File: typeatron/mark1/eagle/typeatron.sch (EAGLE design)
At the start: 24 parts

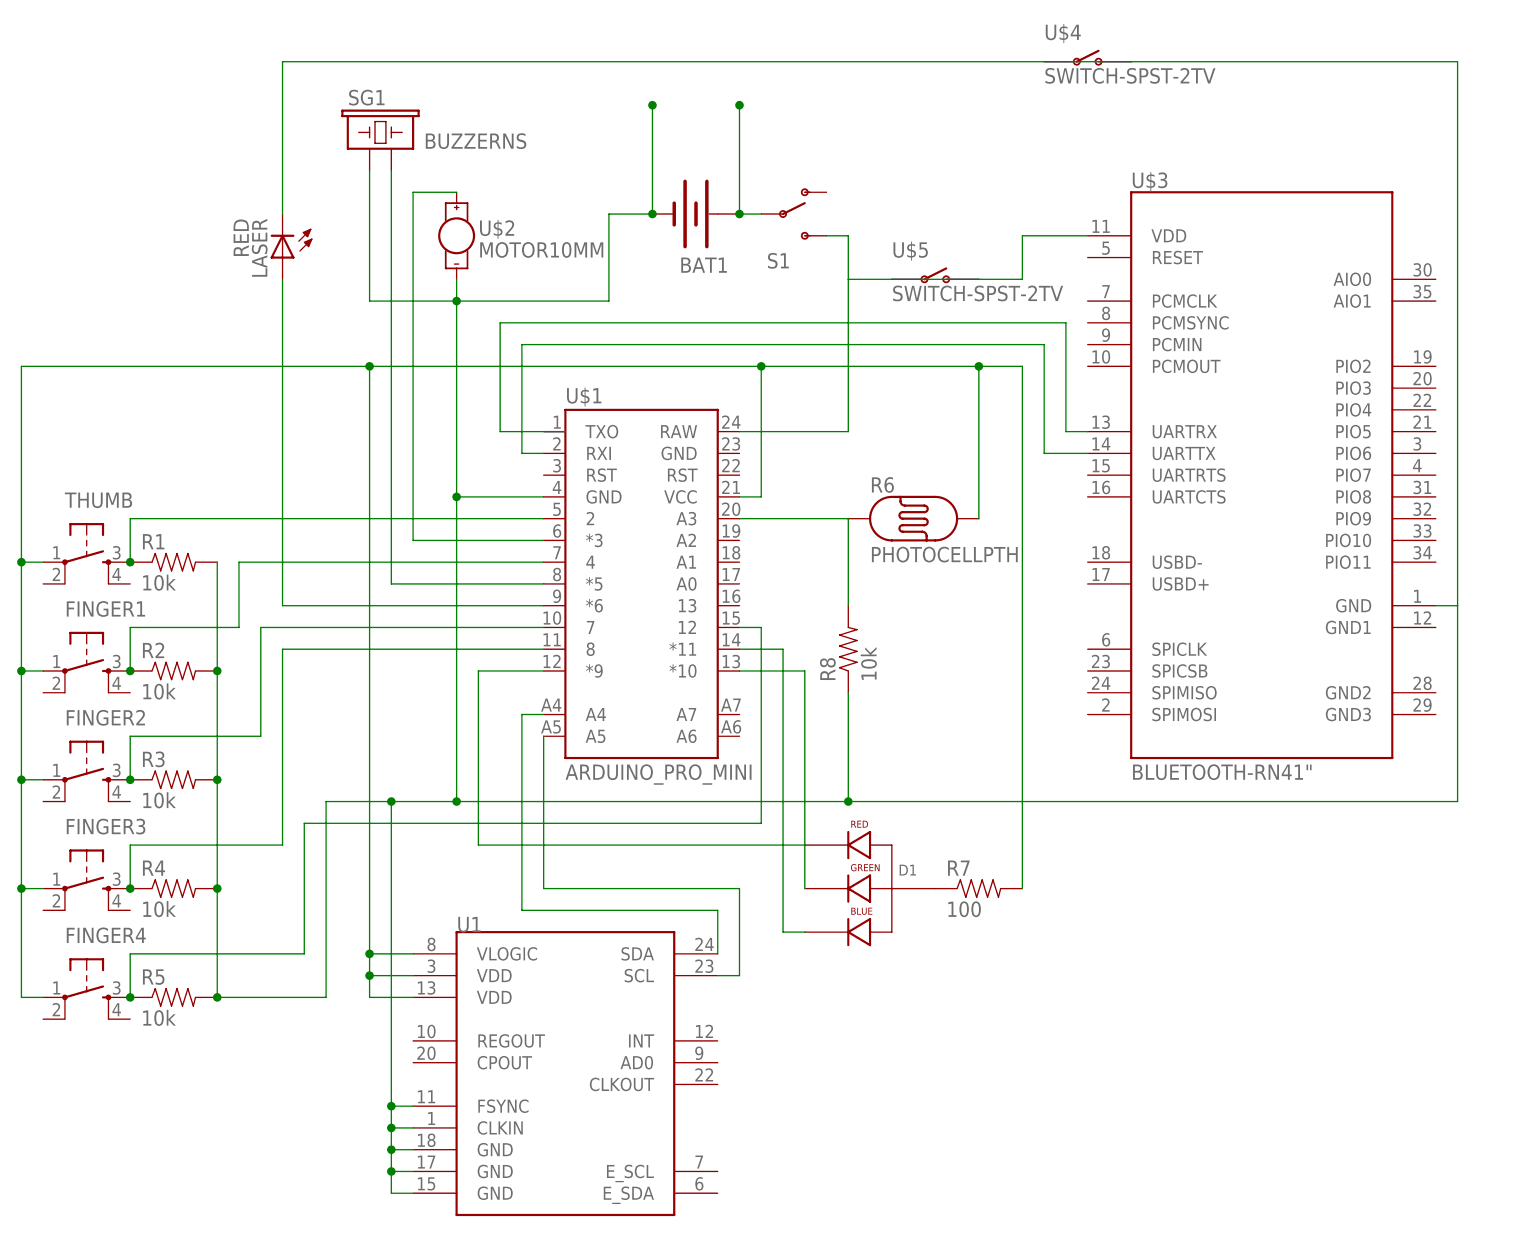
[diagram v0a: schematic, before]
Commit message: Adjusted Typeatron's jumper locations in schematic
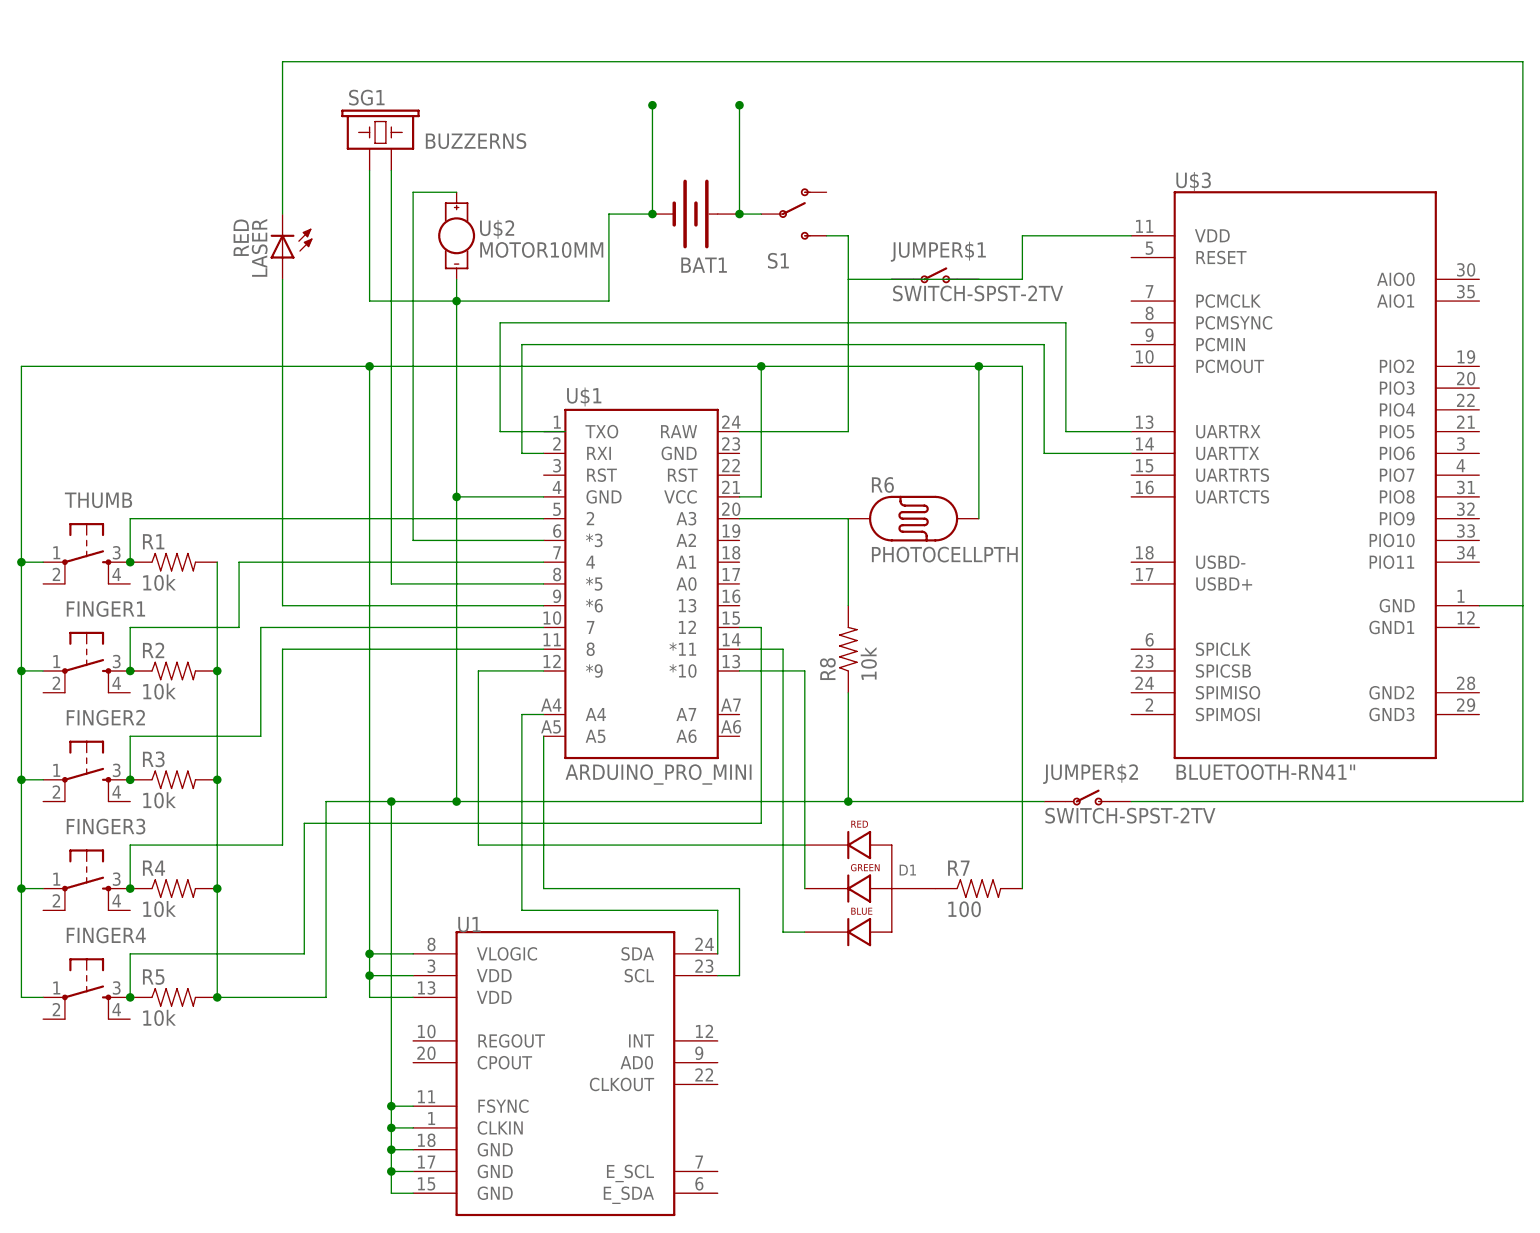
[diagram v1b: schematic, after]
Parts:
- removed U$4: SWITCH-SPST-2TV, SparkFun-Electromechanical:SWITCH-SPST-2TV
- added JUMPER$2: SWITCH-SPST-2TV, SparkFun-Electromechanical:SWITCH-SPST-2TV
- renumbered U$5 to JUMPER$1
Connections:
- new net N$9: JUMPER$2.O, LASER.C, U$3.GND
- net N$3: now also JUMPER$2.P; no longer LASER.C, U$3.GND, U$4.O, U$4.P
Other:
- moved on the sheet: U$3
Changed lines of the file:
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@@
 <part name="R8" library="SparkFun-Resistors" deviceset="10KOHM1/6W5%(PTH)" device="KIT" value="10k"/>
 <part name="LASER" library="SparkFun-LED" deviceset="LED-RED" device="0603" value="RED"/>
-<part name="U$4" library="SparkFun-Electromechanical" deviceset="SWITCH-SPST-2" device="TV"/>
-<part name="U$5" library="SparkFun-Electromechanical" deviceset="SWITCH-SPST-2" device="TV"/>
+<part name="JUMPER$1" library="SparkFun-Electromechanical" deviceset="SWITCH-SPST-2" device="TV"/>
+<part name="JUMPER$2" library="SparkFun-Electromechanical" deviceset="SWITCH-SPST-2" device="TV"/>
 </parts>
 <sheets>
@@
 <instance part="SG1" gate="G$1" x="30.48" y="114.3"/>
 <instance part="U$2" gate="G$1" x="40.64" y="104.14"/>
-<instance part="U$3" gate="G$1" x="134.62" y="76.2"/>
+<instance part="U$3" gate="G$1" x="139.7" y="76.2"/>
 <instance part="BAT1" gate="G$1" x="68.58" y="106.68" rot="R180"/>
 <instance part="R6" gate="G$1" x="93.98" y="71.12"/>
@@
 <instance part="R8" gate="G$1" x="86.36" y="55.88" rot="R90"/>
 <instance part="LASER" gate="G$1" x="20.32" y="101.6" rot="R180"/>
-<instance part="U$4" gate="G$1" x="114.3" y="124.46"/>
-<instance part="U$5" gate="G$1" x="96.52" y="99.06"/>
+<instance part="JUMPER$1" gate="G$1" x="96.52" y="99.06"/>
+<instance part="JUMPER$2" gate="G$1" x="114.3" y="38.1"/>
 </instances>
 <busses>
@@
 <wire x1="83.82" y1="104.14" x2="86.36" y2="104.14" width="0.1524" layer="91"/>
 <wire x1="86.36" y1="104.14" x2="86.36" y2="99.06" width="0.1524" layer="91"/>
-<pinref part="U$5" gate="G$1" pin="O"/>
-<pinref part="U$5" gate="G$1" pin="P"/>
+<pinref part="JUMPER$1" gate="G$1" pin="O"/>
+<pinref part="JUMPER$1" gate="G$1" pin="P"/>
 <wire x1="91.44" y1="99.06" x2="101.6" y2="99.06" width="0.1524" layer="91"/>
 <wire x1="86.36" y1="99.06" x2="91.44" y2="99.06" width="0.1524" layer="91"/>
@@
 <wire x1="106.68" y1="99.06" x2="106.68" y2="104.14" width="0.1524" layer="91"/>
 <pinref part="U$3" gate="G$1" pin="VDD"/>
-<wire x1="106.68" y1="104.14" x2="114.3" y2="104.14" width="0.1524" layer="91"/>
+<wire x1="106.68" y1="104.14" x2="119.38" y2="104.14" width="0.1524" layer="91"/>
 </segment>
 </net>
@@
 <segment>
 <pinref part="U$3" gate="G$1" pin="UARTTX"/>
-<wire x1="114.3" y1="78.74" x2="109.22" y2="78.74" width="0.1524" layer="91"/>
+<wire x1="119.38" y1="78.74" x2="109.22" y2="78.74" width="0.1524" layer="91"/>
 <wire x1="109.22" y1="78.74" x2="109.22" y2="91.44" width="0.1524" layer="91"/>
 <wire x1="109.22" y1="91.44" x2="48.26" y2="91.44" width="0.1524" layer="91"/>
@@
 <segment>
 <pinref part="U$3" gate="G$1" pin="UARTRX"/>
-<wire x1="114.3" y1="81.28" x2="111.76" y2="81.28" width="0.1524" layer="91"/>
+<wire x1="119.38" y1="81.28" x2="111.76" y2="81.28" width="0.1524" layer="91"/>
 <wire x1="111.76" y1="81.28" x2="111.76" y2="93.98" width="0.1524" layer="91"/>
 <wire x1="111.76" y1="93.98" x2="45.72" y2="93.98" width="0.1524" layer="91"/>
@@
 <wire x1="50.8" y1="73.66" x2="40.64" y2="73.66" width="0.1524" layer="91"/>
 <junction x="40.64" y="73.66"/>
-<pinref part="U$3" gate="G$1" pin="GND"/>
-<wire x1="86.36" y1="38.1" x2="157.48" y2="38.1" width="0.1524" layer="91"/>
-<wire x1="157.48" y1="38.1" x2="157.48" y2="60.96" width="0.1524" layer="91"/>
-<wire x1="157.48" y1="60.96" x2="154.94" y2="60.96" width="0.1524" layer="91"/>
-<pinref part="LASER" gate="G$1" pin="C"/>
-<wire x1="20.32" y1="106.68" x2="20.32" y2="124.46" width="0.1524" layer="91"/>
-<wire x1="20.32" y1="124.46" x2="109.22" y2="124.46" width="0.1524" layer="91"/>
-<wire x1="109.22" y1="124.46" x2="119.38" y2="124.46" width="0.1524" layer="91"/>
-<wire x1="119.38" y1="124.46" x2="157.48" y2="124.46" width="0.1524" layer="91"/>
-<wire x1="157.48" y1="124.46" x2="157.48" y2="60.96" width="0.1524" layer="91"/>
-<pinref part="U$4" gate="G$1" pin="P"/>
-<pinref part="U$4" gate="G$1" pin="O"/>
+<wire x1="86.36" y1="38.1" x2="109.22" y2="38.1" width="0.1524" layer="91"/>
+<pinref part="JUMPER$2" gate="G$1" pin="P"/>
 </segment>
 </net>
@@
 </segment>
 </net>
+<net name="N$9" class="0">
+<segment>
+<pinref part="LASER" gate="G$1" pin="C"/>
+<wire x1="20.32" y1="106.68" x2="20.32" y2="124.46" width="0.1524" layer="91"/>
+<wire x1="20.32" y1="124.46" x2="165.1" y2="124.46" width="0.1524" layer="91"/>
+<pinref part="JUMPER$2" gate="G$1" pin="O"/>
+<wire x1="119.38" y1="38.1" x2="165.1" y2="38.1" width="0.1524" layer="91"/>
+<wire x1="165.1" y1="124.46" x2="165.1" y2="60.96" width="0.1524" layer="91"/>
+<pinref part="U$3" gate="G$1" pin="GND"/>
+<wire x1="165.1" y1="60.96" x2="165.1" y2="38.1" width="0.1524" layer="91"/>
+<wire x1="160.02" y1="60.96" x2="165.1" y2="60.96" width="0.1524" layer="91"/>
+</segment>
+</net>
